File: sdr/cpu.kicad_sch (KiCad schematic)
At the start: 30 parts, among them J2 Conn_01x06, SW1 RESET, SW2 KEY, SW3 PTT, U4 CH32V305RBT6, Y2 25MHz

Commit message: Complete layout
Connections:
- net TXMIX_EN: now reaches U4.41 (PA8)
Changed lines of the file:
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@@
+    (stroke (width 0) (type default))
+  )
+  (wire (pts (xy 153.67 101.6) (xy 160.02 101.6))
     (stroke (width 0) (type default))
   )
@@
       (effects (font (size 1.27 1.27)) (justify left) hide)
     )
+  )
+  (global_label "TXMIX_EN" (shape input) (at 160.02 101.6 0) (fields_autoplaced)
+    (effects (font (size 1.27 1.27)) (justify left))
+    (property "Intersheetrefs" "${INTERSHEET_REFS}" (at 171.8157 101.6 0)
+      (effects (font (size 1.27 1.27)) (justify left) hide)
+    )

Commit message: First version 0.1 completed
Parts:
- added J3: Screen, Connector_PinSocket_2.54mm:PinSocket_1x04_P2.54mm_Vertical, symbol Connector:Conn_01x04_Socket
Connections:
- net +3.3V: now also J3.2 (Pin_2)
- net GND: now also J3.1 (Pin_1)
- net OLED_SCL: now reaches U4.29 (PB10)
- net OLED_SCL: now also J3.3 (Pin_3)
- net OLED_SDA: now reaches U4.30 (PB11)
- net OLED_SDA: now also J3.4 (Pin_4)
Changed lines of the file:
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@@
+    (stroke (width 0) (type default))
+  )
+  (wire (pts (xy 176.53 41.91) (xy 173.99 41.91))
     (stroke (width 0) (type default))
   )
@@
     (stroke (width 0) (type default))
   )
+  (wire (pts (xy 166.37 39.37) (xy 176.53 39.37))
+    (stroke (width 0) (type default))
+  )
   (wire (pts (xy 107.95 60.96) (xy 107.95 64.77))
     (stroke (width 0) (type default))
@@
     (stroke (width 0) (type default))
   )
+  (wire (pts (xy 128.27 139.7) (xy 128.27 140.97))
+    (stroke (width 0) (type default))
+  )
   (wire (pts (xy 192.405 154.305) (xy 192.405 156.845))
     (stroke (width 0) (type default))
@@
     (stroke (width 0) (type default))
   )
+  (wire (pts (xy 125.73 139.7) (xy 125.73 140.97))
+    (stroke (width 0) (type default))
+  )
   (wire (pts (xy 76.2 96.52) (xy 54.61 96.52))
     (stroke (width 0) (type default))
@@
   )
   (wire (pts (xy 97.79 52.07) (xy 92.075 52.07))
+    (stroke (width 0) (type default))
+  )
+  (wire (pts (xy 173.99 41.91) (xy 173.99 36.83))
     (stroke (width 0) (type default))
   )
@@
     (effects (font (size 1.27 1.27)) (justify left bottom))
   )
+  (global_label "OLED_SDA" (shape input) (at 176.53 46.99 180) (fields_autoplaced)
+    (effects (font (size 1.27 1.27)) (justify right))
+    (property "Intersheetrefs" "${INTERSHEET_REFS}" (at 164.3109 46.99 0)
+      (effects (font (size 1.27 1.27)) (justify right) hide)
+    )
+  )
   (global_label "NRST" (shape input) (at 226.06 76.2 180) (fields_autoplaced)
     (effects (font (size 1.27 1.27)) (justify right))
@@
     )
   )
+  (global_label "OLED_SDA" (shape input) (at 128.27 140.97 270) (fields_autoplaced)
+    (effects (font (size 1.27 1.27)) (justify right))
+    (property "Intersheetrefs" "${INTERSHEET_REFS}" (at 128.27 153.1891 90)
+      (effects (font (size 1.27 1.27)) (justify right) hide)
+    )
+  )
   (global_label "SWCLK" (shape input) (at 133.35 57.15 90) (fields_autoplaced)
     (effects (font (size 1.27 1.27)) (justify left))
@@
     )
   )
+  (global_label "OLED_SCL" (shape input) (at 125.73 140.97 270) (fields_autoplaced)
+    (effects (font (size 1.27 1.27)) (justify right))
+    (property "Intersheetrefs" "${INTERSHEET_REFS}" (at 125.73 153.1286 90)
+      (effects (font (size 1.27 1.27)) (justify right) hide)
+    )
+  )
   (global_label "SPI_MISO" (shape input) (at 172.085 116.84 0) (fields_autoplaced)
     (effects (font (size 1.27 1.27)) (justify left))
@@
     (property "Intersheetrefs" "${INTERSHEET_REFS}" (at 167.0293 88.8206 0)
       (effects (font (size 1.27 1.27)) (justify left) hide)
+    )
+  )
+  (global_label "OLED_SCL" (shape input) (at 176.53 44.45 180) (fields_autoplaced)
+    (effects (font (size 1.27 1.27)) (justify right))
+    (property "Intersheetrefs" "${INTERSHEET_REFS}" (at 164.3714 44.45 0)
+      (effects (font (size 1.27 1.27)) (justify right) hide)
     )
   )
@@
     )
   )
+  (symbol (lib_id "Connector:Conn_01x04_Socket") (at 181.61 41.91 0) (unit 1)
+    (in_bom yes) (on_board yes) (dnp no) (fields_autoplaced)
+    (property "Reference" "J3" (at 183.515 42.545 0)
+      (effects (font (size 1.27 1.27)) (justify left))
+    )
+    (property "Value" "Screen" (at 183.515 45.085 0)
+      (effects (font (size 1.27 1.27)) (justify left))
+    )
+    (property "Footprint" "Connector_PinSocket_2.54mm:PinSocket_1x04_P2.54mm_Vertical" (at 181.61 41.91 0)
+      (effects (font (size 1.27 1.27)) hide)
+    )
+    (property "Datasheet" "~" (at 181.61 41.91 0)
+      (effects (font (size 1.27 1.27)) hide)
+    )
+    (pin "1")
+    (pin "2")
+    (pin "3")
+    (pin "4")
+    (instances
+      (project "attorv"
+        (path "/6109b252-c3cf-4e79-aa0f-a13bf7f36f08"
+          (reference "J3") (unit 1)
+        )
+      )
+      (project "sdr"
+        (path "/ee974380-b45b-4b16-8475-50e4e51dc6cf/ad7b2242-3b39-40b3-b2e9-d6ea800dea9e"
+          (reference "J5") (unit 1)
+        )
+      )
+    )
+  )
   (symbol (lib_id "power:GND") (at 41.91 124.46 0) (unit 1)
     (in_bom yes) (on_board yes) (dnp no) (fields_autoplaced)
@@
     )
   )
+  (symbol (lib_id "power:GND") (at 166.37 39.37 270) (unit 1)
+    (in_bom yes) (on_board yes) (dnp no) (fields_autoplaced)
+    (property "Reference" "#PWR017" (at 160.02 39.37 0)
+      (effects (font (size 1.27 1.27)) hide)
+    )
+    (property "Value" "GND" (at 162.56 40.005 90)
+      (effects (font (size 1.27 1.27)) (justify right))
+    )
+    (property "Footprint" "" (at 166.37 39.37 0)
+      (effects (font (size 1.27 1.27)) hide)
+    )
+    (property "Datasheet" "" (at 166.37 39.37 0)
+      (effects (font (size 1.27 1.27)) hide)
+    )
+    (property "JLCPCB" "C2296" (at 166.37 39.37 0)
+      (effects (font (size 1.27 1.27)) hide)
+    )
+    (pin "1")
+    (instances
+      (project "attorv"
+        (path "/6109b252-c3cf-4e79-aa0f-a13bf7f36f08"
+          (reference "#PWR017") (unit 1)
+        )
+      )
+      (project "batomatic"
+        (path "/6a22bd48-0d2f-47d1-9720-f349a7ed8e38"
+          (reference "#PWR0102") (unit 1)
+        )
+      )
+      (project "sdr"
+        (path "/ee974380-b45b-4b16-8475-50e4e51dc6cf/ad7b2242-3b39-40b3-b2e9-d6ea800dea9e"
+          (reference "#PWR056") (unit 1)
+        )
+      )
+    )
+  )
   (symbol (lib_id "power:GND") (at 85.09 168.91 0) (unit 1)
     (in_bom yes) (on_board yes) (dnp no) (fields_autoplaced)
@@
         )
       )
+    )
+  )
+  (symbol (lib_id "power:+3.3V") (at 173.99 36.83 0) (unit 1)
+    (in_bom yes) (on_board yes) (dnp no) (fields_autoplaced)
+    (property "Reference" "#PWR018" (at 173.99 40.64 0)
+      (effects (font (size 1.27 1.27)) hide)
+    )
+    (property "Value" "+3.3V" (at 173.99 31.75 0)
+      (effects (font (size 1.27 1.27)))
+    )
+    (property "Footprint" "" (at 173.99 36.83 0)
+      (effects (font (size 1.27 1.27)) hide)
+    )
+    (property "Datasheet" "" (at 173.99 36.83 0)
+      (effects (font (size 1.27 1.27)) hide)
+    )
+    (pin "1")
+    (instances
+      (project "attorv"
+        (path "/6109b252-c3cf-4e79-aa0f-a13bf7f36f08"
+          (reference "#PWR018") (unit 1)
+        )
+      )
+      (project "batomatic"
+        (path "/6a22bd48-0d2f-47d1-9720-f349a7ed8e38"
+          (reference "#PWR017") (unit 1)
+        )
+      )
+      (project "sdr"
+        (path "/ee974380-b45b-4b16-8475-50e4e51dc6cf/ad7b2242-3b39-40b3-b2e9-d6ea800dea9e"
+          (reference "#PWR059") (unit 1)
+        )
+      )

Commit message: Update the via size. Reduce footprints outside board.
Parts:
- J2: footprint Connector_PinHeader_2.54mm:PinHeader_1x06_P2.54mm_Horizontal -> Connector_PinHeader_2.54mm:PinHeader_1x06_P2.54mm_Vertical
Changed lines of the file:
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@@
       (effects (font (size 1.27 1.27)) (justify left))
     )
-    (property "Footprint" "Connector_PinHeader_2.54mm:PinHeader_1x06_P2.54mm_Horizontal" (at 250.19 71.12 0)
+    (property "Footprint" "Connector_PinHeader_2.54mm:PinHeader_1x06_P2.54mm_Vertical" (at 250.19 71.12 0)
       (effects (font (size 1.27 1.27)) hide)
     )

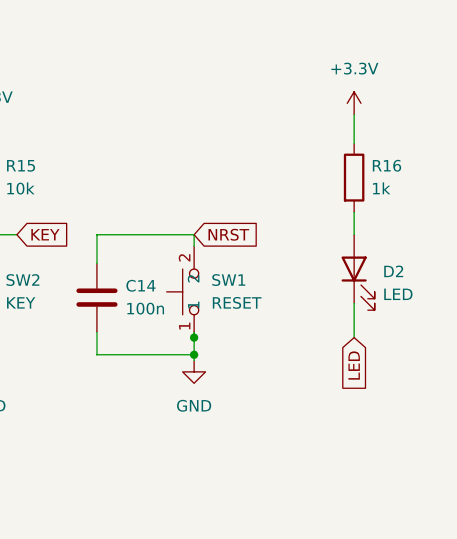
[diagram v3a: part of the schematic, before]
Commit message: Added code first draft
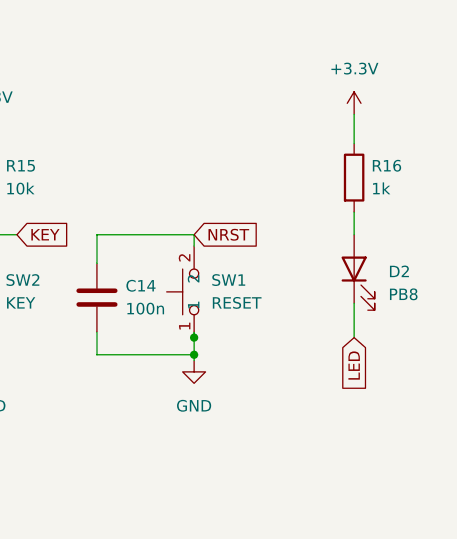
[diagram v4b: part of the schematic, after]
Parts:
- D2: value LED -> PB8
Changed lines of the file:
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@@
   (symbol (lib_id "Device:LED") (at 267.97 147.32 90) (unit 1)
     (in_bom yes) (on_board yes) (dnp no) (fields_autoplaced)
-    (property "Reference" "D2" (at 271.145 147.6374 90)
+    (property "Reference" "D2" (at 271.78 147.6375 90)
       (effects (font (size 1.27 1.27)) (justify right))
     )
-    (property "Value" "LED" (at 271.145 150.1774 90)
+    (property "Value" "PB8" (at 271.78 150.1775 90)
       (effects (font (size 1.27 1.27)) (justify right))
     )

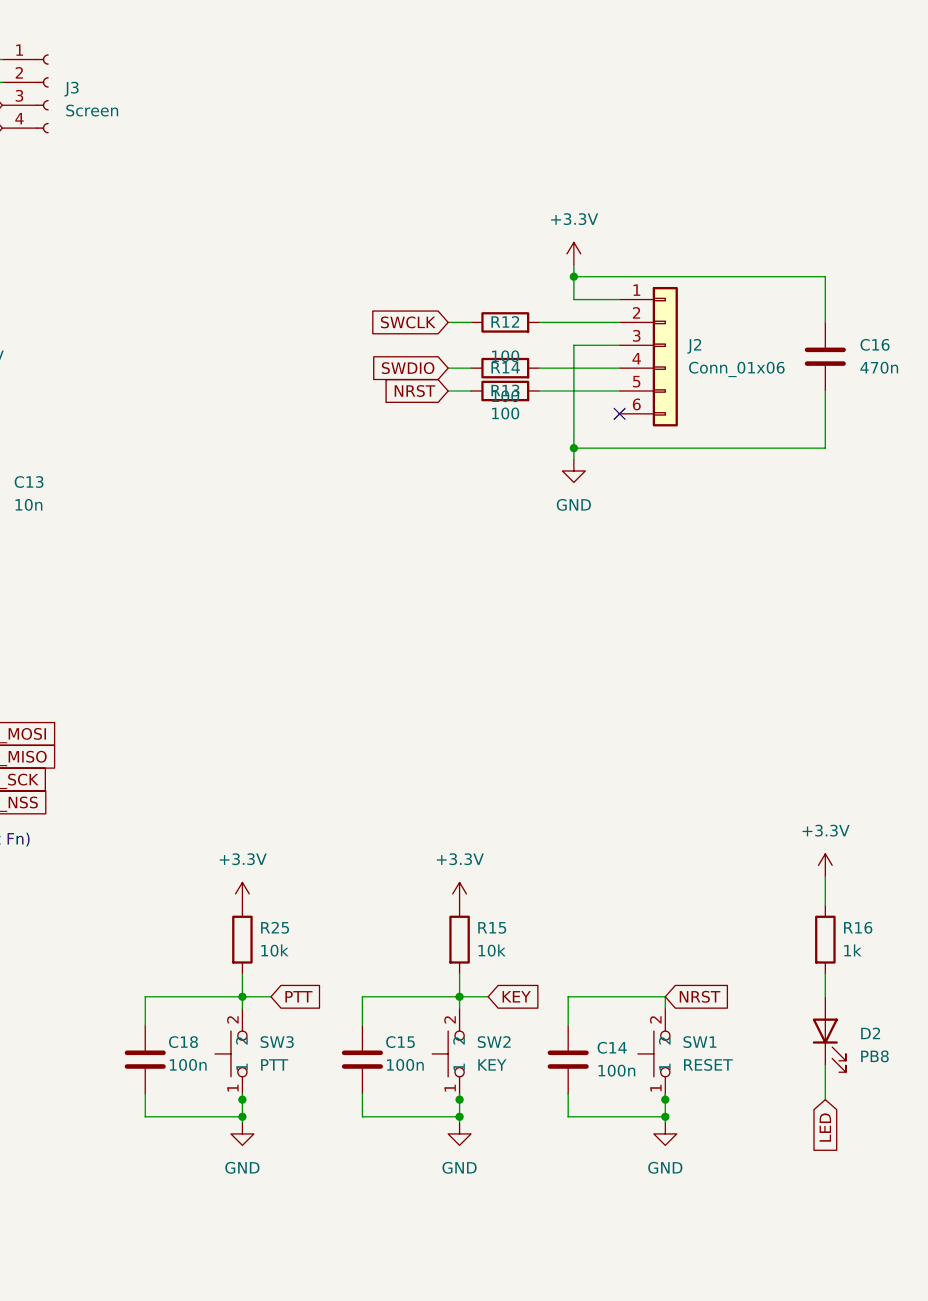
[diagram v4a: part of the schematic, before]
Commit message: Update footprints, and add an swd-connect-5
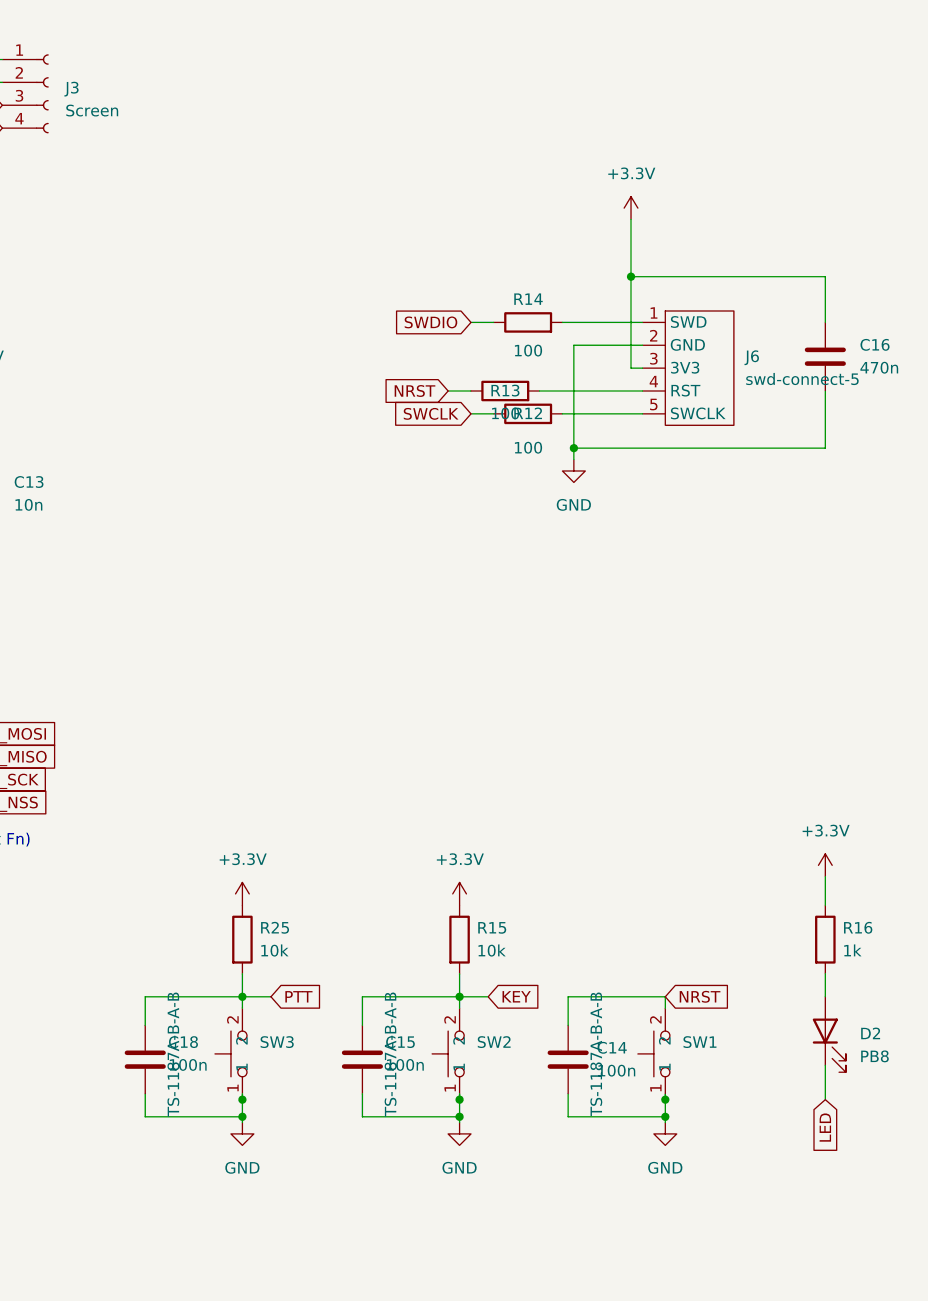
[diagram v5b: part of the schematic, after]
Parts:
- removed J2: Conn_01x06, Connector_PinHeader_2.54mm:PinHeader_1x06_P2.54mm_Vertical, symbol Connector_Generic:Conn_01x06
- added J6: swd-connect-5, swd-connect:swd-connect-5-mcu, symbol swd-connect:swd-connect-5
- SW1: value RESET -> TS-1187A-B-A-B
- SW2: value KEY -> TS-1187A-B-A-B
- SW3: value PTT -> TS-1187A-B-A-B
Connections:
- net +3.3V: now also J6.3 (3V3)
- net GND: now also J6.2 (GND)
- net at R12.2: now also J6.5 (SWCLK)
- net at R13.2: now also J6.4 (RST)
- net at R14.2: now also J6.1 (SWD)
- no-connect marks 1 -> 0
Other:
- moved on the sheet: R12, R14

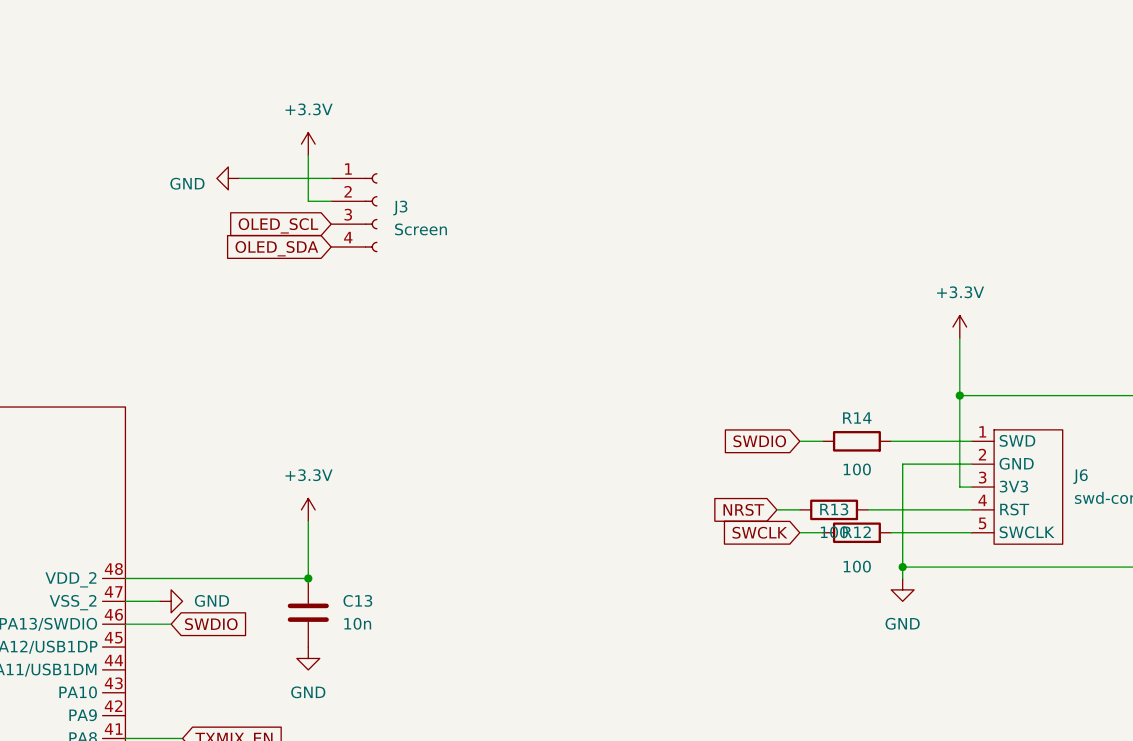
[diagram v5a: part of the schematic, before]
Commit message: Added extra pullup resistors on the OLED i2C. Changed the Synthesizer pullups to 2.2k from 10k
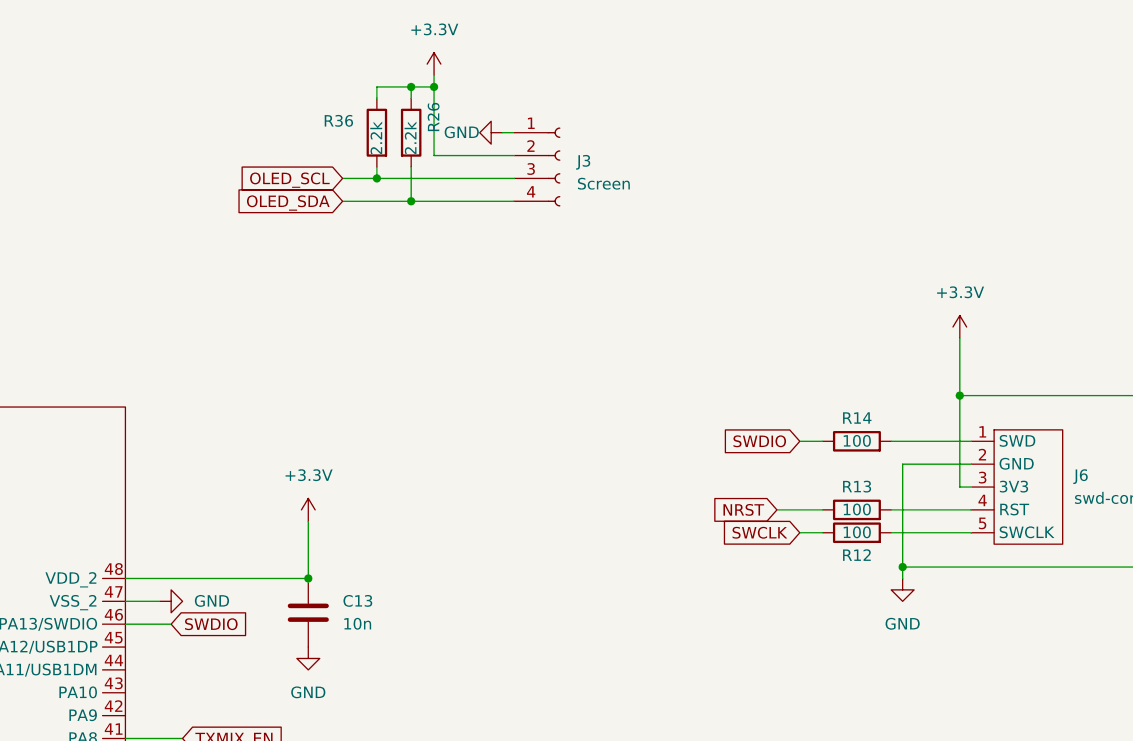
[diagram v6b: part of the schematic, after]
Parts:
- added R26, R36: 2.2k, symbol Device:R
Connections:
- net +3.3V: now also R26.1, R36.1
- net OLED_SCL: now also R36.2
- net OLED_SDA: now also R26.2
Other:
- moved on the sheet: J3, R13
